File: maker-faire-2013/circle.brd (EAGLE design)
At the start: 38.1 x 38.1 mm, 11 parts, among them Q1 2N3904, Q2 2N3904

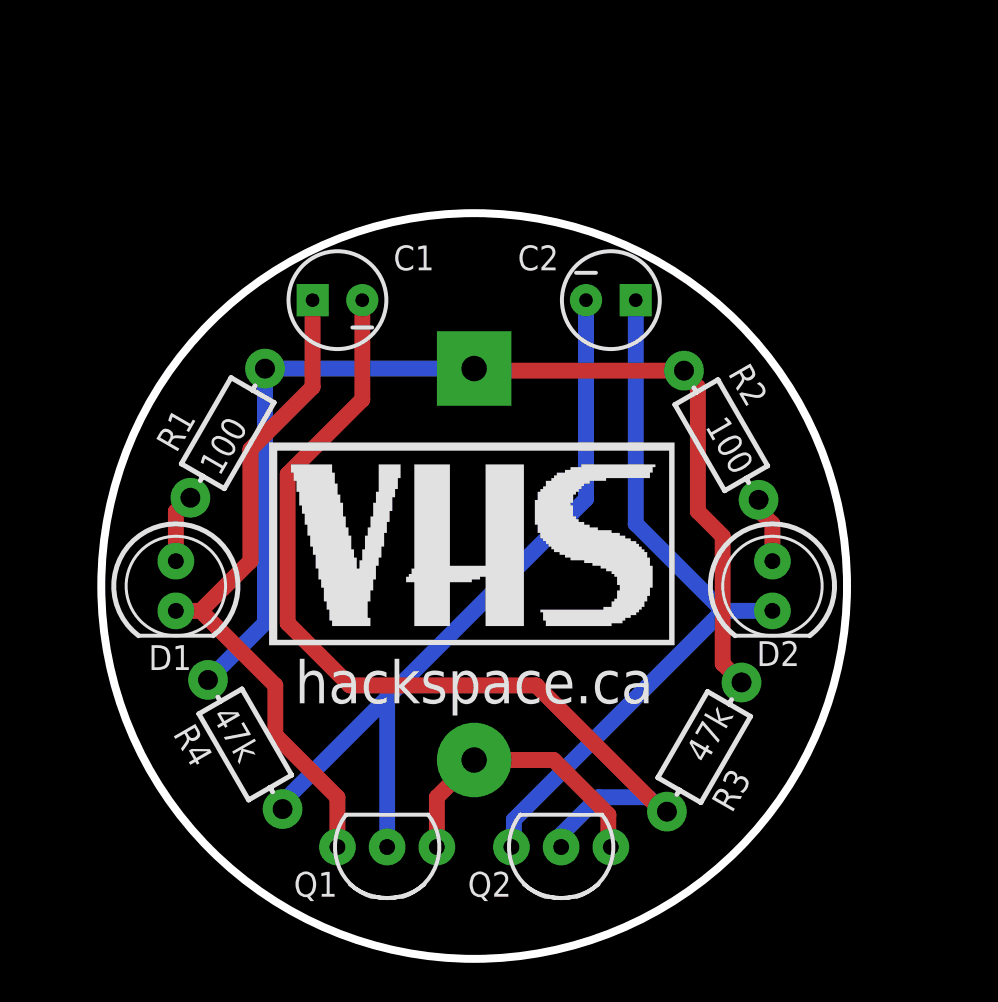
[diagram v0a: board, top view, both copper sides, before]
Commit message: Updated with 0.2" caps and power switch
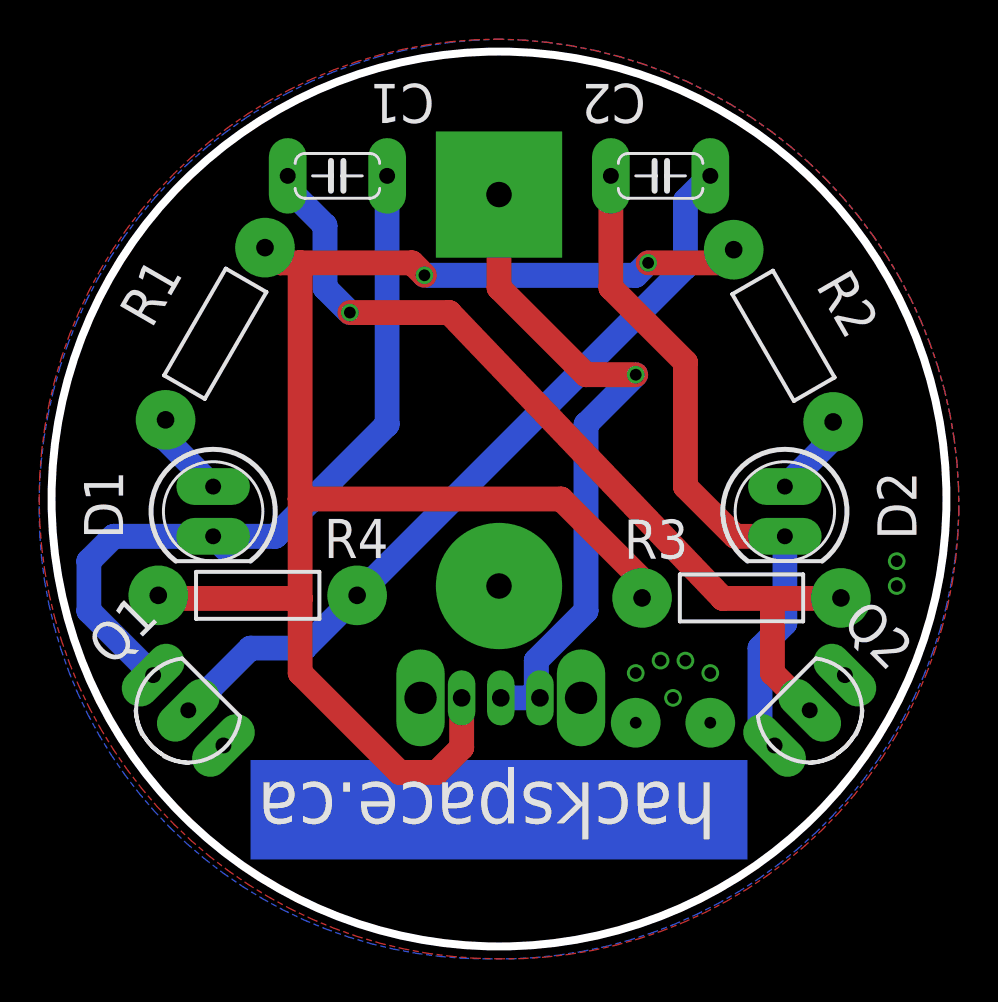
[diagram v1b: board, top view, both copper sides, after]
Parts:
- added BADGECLIP: BADGE_CLIP, circle:BADGE_CLIP
- added U$1: (no value), circle:VHS-LOGO-SMALL
- added U$2: 0S102011MS2QN1, circle:0S102011MS2QN1
- BATTERY: device SparkFun-Electromechanical:BATTCOM_20MM_PTH -> circle:BATTCOM_20MM_PTH
- C1, C2: device SparkFun-Passives:CPOL-RADIAL-10UF-25V -> circle:C050-024X044
- D1, D2: device SparkFun-LED:LED5MM-KIT -> circle:LED5MM-KIT
- Q1, Q2: device SparkFun-DiscreteSemi:TO-92-AMMO -> circle:TO-92-AMMO
- R1, R2, R3, R4: device SparkFun-Resistors:AXIAL-0.3-KIT -> circle:AXIAL-0.4
- moved Q2 14.5 mm to (37.5, 10.2), turned to 225 degrees
- moved Q1 12.3 mm to (5.71, 10.2), turned to 135 degrees
- moved BATTERY 8.98 mm to (21.6, 16.5)
- moved R3 7.85 mm to (34.0, 15.9), turned to 0 degrees
- moved R4 7.65 mm to (9.26, 16.0), turned to 0 degrees
- moved C2 6.84 mm to (29.8, 37.5)
- moved C1 6.35 mm to (13.3, 37.5)
- moved R2 5.99 mm to (36.1, 29.3)
- moved R1 5.12 mm to (7.09, 29.4)
- moved D1 4.26 mm to (6.99, 20.3)
- moved D2 3.86 mm to (36.2, 20.3)
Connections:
- new net N$1: BATTERY.1, U$2.1, U$2.2
- net GND: now also BADGECLIP.1
- net VCC: now also U$2.3; no longer BATTERY.1
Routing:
- net N$1: track 0.00 -> 34.2 mm, vias 0 -> 1
- net VCC: track 55.7 -> 86.9 mm, vias 0 -> 2
- net GND: track 15.0 -> 0.00 mm, vias 0 -> 9
- net N$4: track 34.5 -> 38.9 mm
- net N$7: track 48.5 -> 46.1 mm, vias 0 -> 1
- net N$3: track 36.9 -> 35.1 mm
- net N$8: track 3.40 -> 4.33 mm
- net N$10: track 3.56 -> 4.42 mm
- added copper zone on layer 1, net GND
- removed copper zone on layer 1, net VCC
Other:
- board size 38.1 x 38.1 mm -> 45.7 x 45.7 mm
- board text removed: "CR2032"

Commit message: Change caps to 0.2 pitch, fix silk issues, panelise into 4 per 10x10 panel
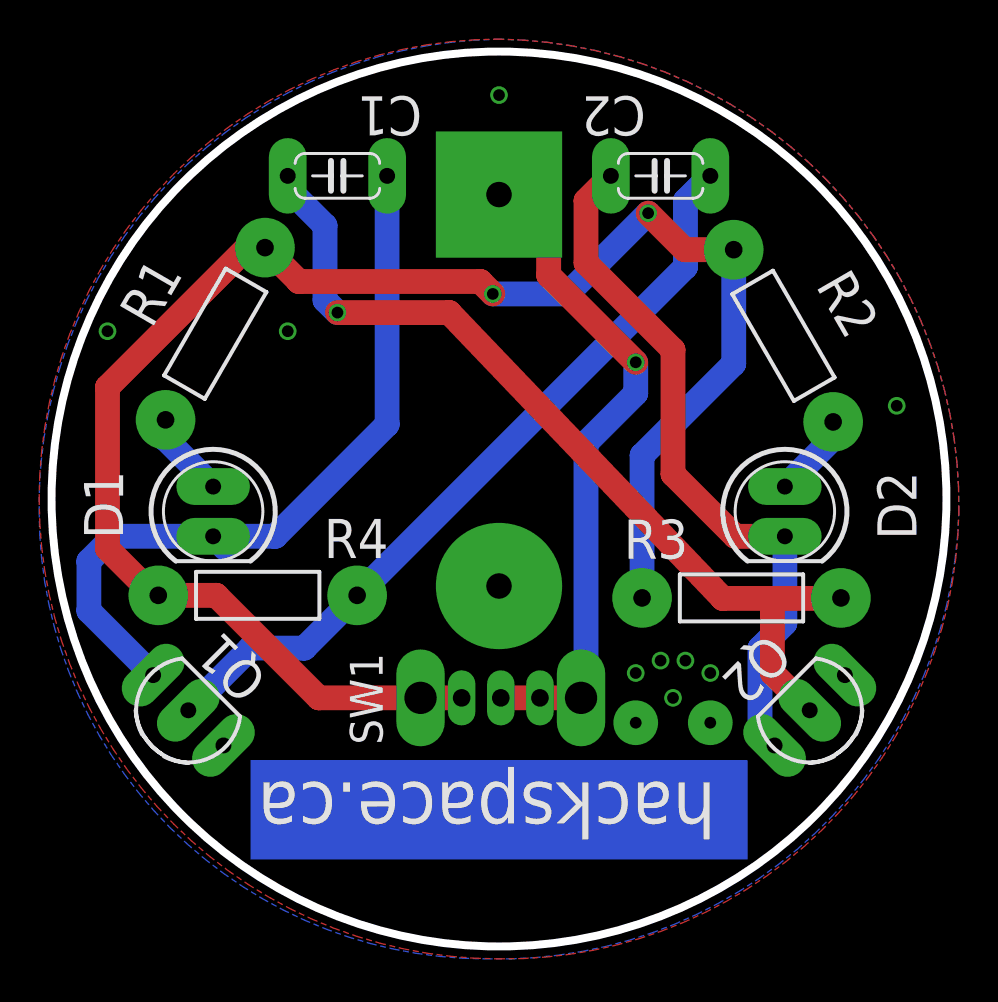
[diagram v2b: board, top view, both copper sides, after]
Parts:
- R1, R2: value 100 -> 100R
- renumbered U$2 to SW1
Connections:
- removed net N$1: BATTERY.1, SW1.1, SW1.2
- removed net VCC: R1.P$2, R2.P$2, R3.P$1, R4.P$1, SW1.3
- new net CASE1: BATTERY.1, SW1.1, SW1.2, SW1.CASE1
- new net CASE2: R1.P$2, R2.P$2, R3.P$1, R4.P$1, SW1.3, SW1.CASE2
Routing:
- net CASE2: track 0.00 -> 87.6 mm, vias 0 -> 2
- net VCC: track 86.9 -> 0.00 mm, vias 2 -> 0
- net CASE1: track 0.00 -> 34.2 mm, vias 0 -> 1
- net N$1: track 34.2 -> 0.00 mm, vias 1 -> 0
- net N$3: track 35.1 -> 36.2 mm
